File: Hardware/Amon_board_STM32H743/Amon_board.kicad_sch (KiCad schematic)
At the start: 28 parts, among them J1 USB2.0_C_Rev, SW1 SW_DPDT, SW2 SW_SPST, U1 USBLC6-2P6, U2 STM32F405RGT6-LQFP64, U3 W25Q128JVS

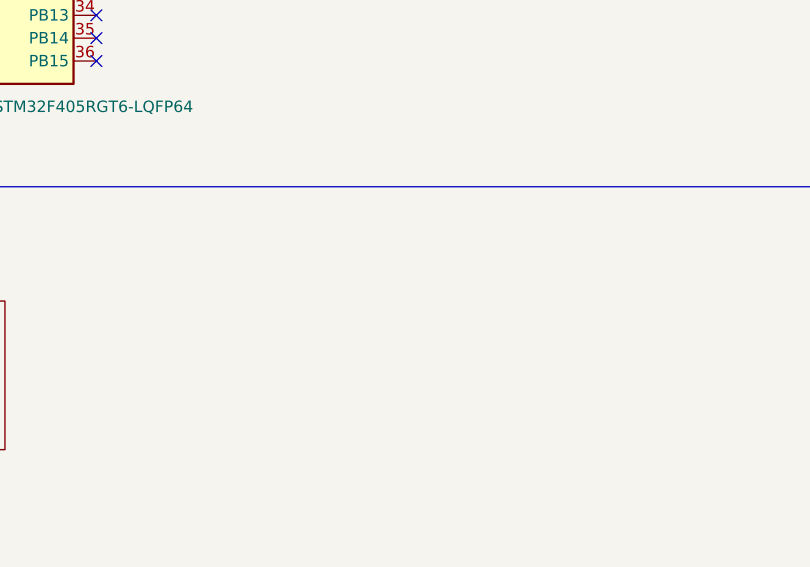
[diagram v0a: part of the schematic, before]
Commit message: Update
added first flight path buffer
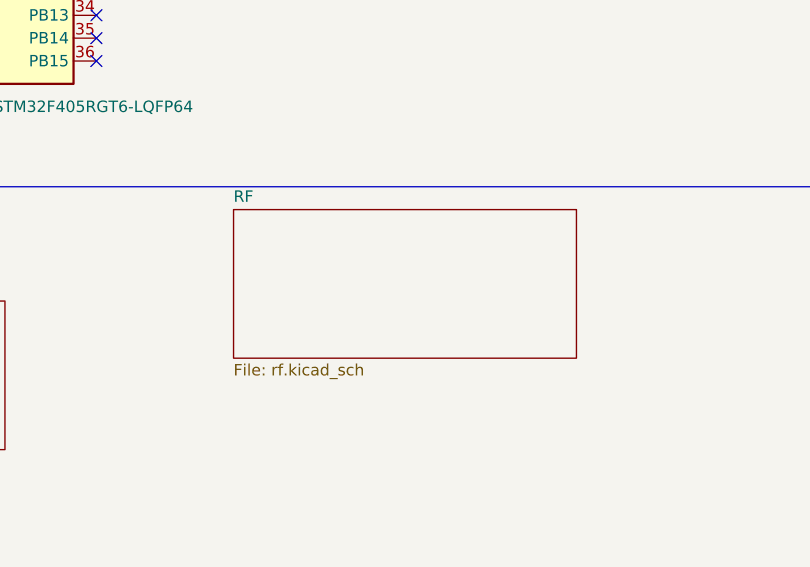
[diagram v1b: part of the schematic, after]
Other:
- added sheet RF (rf.kicad_sch)
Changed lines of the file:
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@@
+	)
+	(sheet
+		(at 193.04 149.86)
+		(size 38.1 16.51)
+		(exclude_from_sim no)
+		(in_bom yes)
+		(on_board yes)
+		(dnp no)
+		(fields_autoplaced yes)
+		(stroke
+			(width 0.1524)
+			(type solid)
+		)
+		(fill
+			(color 0 0 0 0.0000)
+		)
+		(property "Sheetname" "RF"
+			(at 193.04 149.1484 0)
+			(effects
+				(font
+					(size 1.27 1.27)
+				)
+				(justify left bottom)
+			)
+		)
+		(property "Sheetfile" "rf.kicad_sch"
+			(at 193.04 166.9546 0)
+			(effects
+				(font
+					(size 1.27 1.27)
+				)
+				(justify left top)
+			)
+		)
+		(instances
+			(project "Amon_board"
+				(path "/a73fde48-ba79-4d3c-8816-668d8180a86c"
+					(page "5")
+				)
+			)
+		)
 	)
 	(sheet
